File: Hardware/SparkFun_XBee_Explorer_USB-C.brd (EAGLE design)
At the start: 35.6 x 59.7 mm, 106 parts, among them J3 USB Female Type C Connector, J4 QWIIC_RIGHT_ANGLE, U2 AP63203, U5 ESD Diode, U7 FT231XS

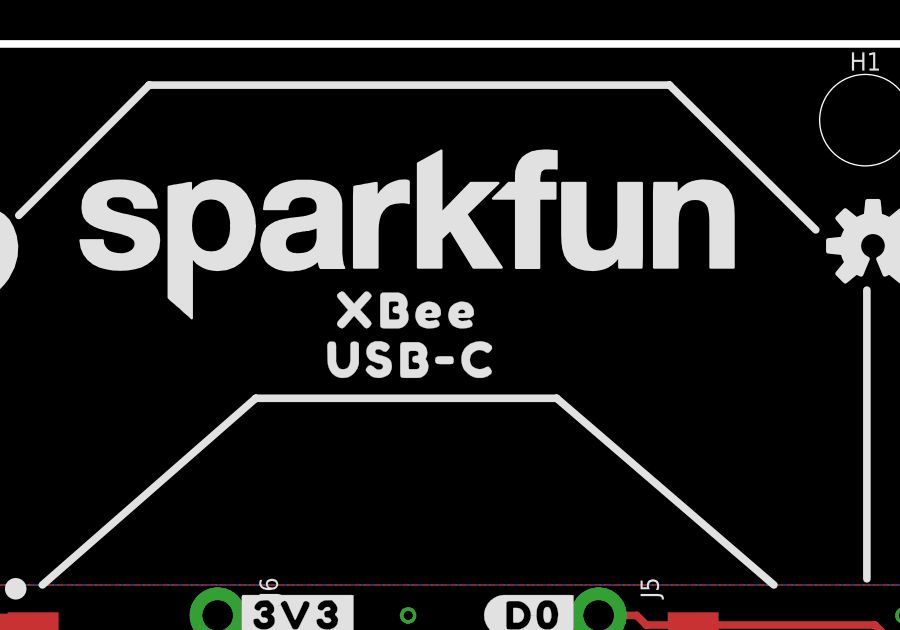
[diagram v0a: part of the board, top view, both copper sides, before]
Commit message: Adds "Explorer" to silk
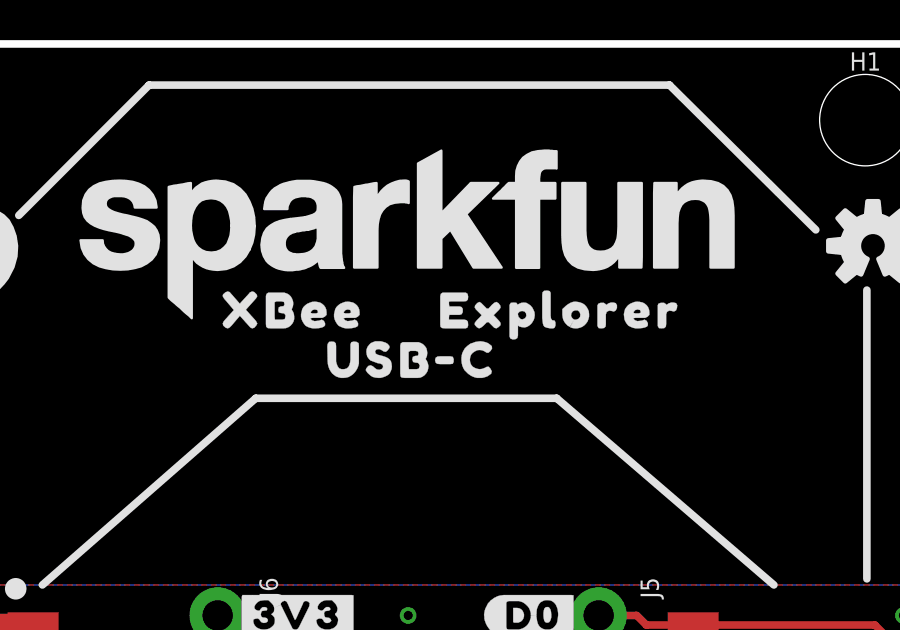
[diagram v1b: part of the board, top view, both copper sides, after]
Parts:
- added U$31, U$32: (no value), top:EXPLORER1344
- moved U$10 3.81 mm to (14.0, 50.8)
- moved U$23 3.81 mm to (21.6, 50.8)
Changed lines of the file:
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@@
 <layers>
 <layer number="1" name="Top" color="4" fill="1" visible="yes" active="yes"/>
-<layer number="2" name="Route2" color="23" fill="1" visible="yes" active="yes"/>
-<layer number="15" name="Route15" color="39" fill="1" visible="yes" active="yes"/>
+<layer number="2" name="Route2" color="23" fill="1" visible="no" active="yes"/>
+<layer number="15" name="Route15" color="39" fill="1" visible="no" active="yes"/>
 <layer number="16" name="Bottom" color="3" fill="1" visible="yes" active="yes"/>
 <layer number="17" name="Pads" color="26" fill="1" visible="yes" active="yes"/>
@@
 <element name="U$3" library="topmirror" package="#GND#0" value="" x="8.763" y="17.78" smashed="yes"/>
 <element name="LOGO1" library="SparkFun-Aesthetics" package="SFE_LOGO_NAME_.2" value="SFE_LOGO_NAME.2_INCH" x="17.78" y="53.34" smashed="yes"/>
-<element name="U$10" library="top" package="XBEE340" value="" x="17.78" y="50.8" smashed="yes"/>
-<element name="U$23" library="top" package="XBEE340" value="" x="17.78" y="50.8" smashed="yes" rot="MR0"/>
+<element name="U$10" library="top" package="XBEE340" value="" x="13.97" y="50.8" smashed="yes"/>
+<element name="U$23" library="top" package="XBEE340" value="" x="21.59" y="50.8" smashed="yes" rot="MR0"/>
 <element name="U$29" library="top" package="ASC32" value="" x="21.209" y="2.413" smashed="yes" rot="R90"/>
 <element name="U$1" library="top" package="RSSI31" value="" x="16.129" y="2.413" smashed="yes" rot="R90"/>
@@
 <element name="LOGO4" library="SparkFun-Aesthetics" package="ORDERING_INSTRUCTIONS" value="SPECIAL_INSTRUCTIONS-ORDERING" x="44.45" y="59.69" smashed="yes"/>
 <element name="U$11" library="topmirror" package="#D1#AD1#SCL#8" value="" x="29.718" y="38.1" smashed="yes" rot="MR0"/>
+<element name="U$31" library="top" package="EXPLORER1344" value="" x="22.86" y="50.8" smashed="yes"/>
+<element name="U$32" library="top" package="EXPLORER1344" value="" x="12.7" y="50.8" smashed="yes" rot="MR0"/>
 </elements>
 <signals>

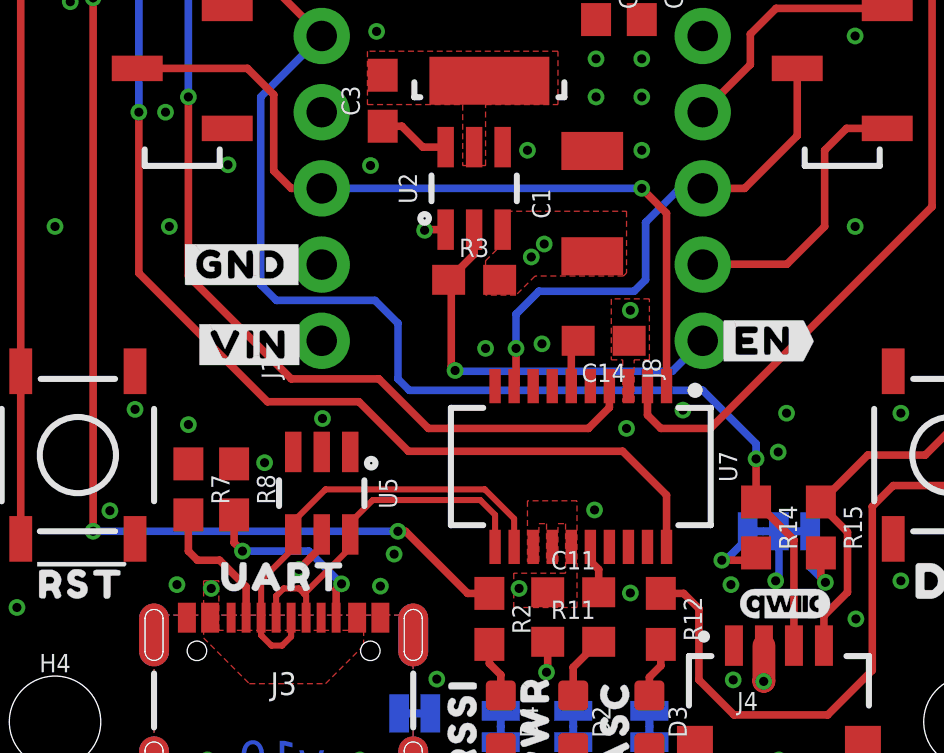
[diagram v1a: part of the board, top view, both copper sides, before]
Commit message: Adds 4.7uF decoupling cap to FTDI
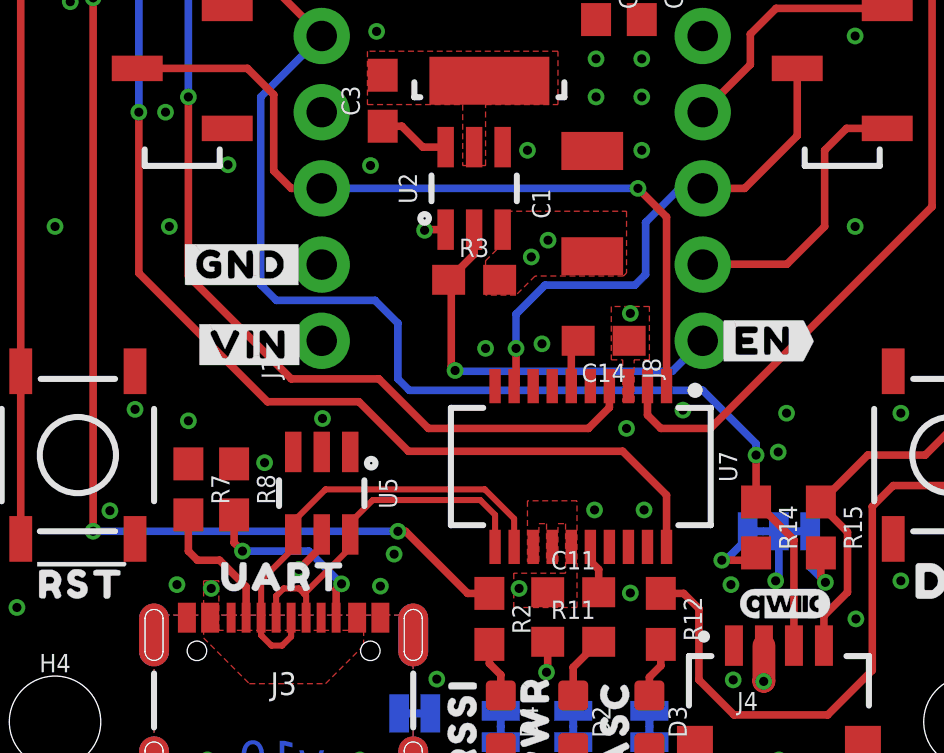
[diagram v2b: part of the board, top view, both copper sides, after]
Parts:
- moved FRAME1 10.2 mm to (-10.2, -26.7)
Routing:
- net GND: vias 74 -> 75
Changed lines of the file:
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@@
 <setting verticaltext="up"/>
 </settings>
-<grid distance="0.05" unitdist="inch" unit="inch" style="dots" multiple="1" display="yes" altdistance="0.005" altunitdist="inch" altunit="inch"/>
+<grid distance="0.05" unitdist="inch" unit="inch" style="dots" multiple="1" display="yes" altdistance="0.001" altunitdist="inch" altunit="inch"/>
 <layers>
 <layer number="1" name="Top" color="4" fill="1" visible="yes" active="yes"/>
-<layer number="2" name="Route2" color="23" fill="1" visible="no" active="yes"/>
-<layer number="15" name="Route15" color="39" fill="1" visible="no" active="yes"/>
+<layer number="2" name="Route2" color="23" fill="1" visible="yes" active="yes"/>
+<layer number="15" name="Route15" color="39" fill="1" visible="yes" active="yes"/>
 <layer number="16" name="Bottom" color="3" fill="1" visible="yes" active="yes"/>
 <layer number="17" name="Pads" color="26" fill="1" visible="yes" active="yes"/>
@@
 <layer number="45" name="Holes" color="7" fill="1" visible="yes" active="yes"/>
 <layer number="46" name="Milling" color="3" fill="1" visible="no" active="yes"/>
-<layer number="47" name="Measures" color="7" fill="1" visible="no" active="yes"/>
+<layer number="47" name="Measures" color="7" fill="1" visible="yes" active="yes"/>
 <layer number="48" name="Document" color="7" fill="1" visible="no" active="yes"/>
 <layer number="49" name="Reference" color="13" fill="1" visible="yes" active="yes"/>
@@
 <wire x1="35.56" y1="0" x2="35.56" y2="59.69" width="0.254" layer="20"/>
 <wire x1="35.56" y1="59.69" x2="0" y2="59.69" width="0.254" layer="20"/>
-<text x="17.78" y="-36.83" size="1.778" layer="51" font="vector">Elias Santistevan</text>
+<text x="17.78" y="-26.67" size="1.778" layer="51" font="vector">Elias Santistevan</text>
 <text x="-19.05" y="-8.89" size="1.778" layer="47" font="vector" ratio="15">Units in Inches</text>
 <text x="11.557" y="0.635" size="1.27" layer="16" font="vector" ratio="15" rot="MR0">v10</text>
@@
 <text x="20.193" y="37.211" size="1.778" layer="15" font="vector" ratio="15">3</text>
 <text x="22.733" y="37.211" size="1.778" layer="16" font="vector" ratio="15" rot="SMR0">4</text>
+<dimension x1="0" y1="0" x2="26.67" y2="0" x3="13.335" y3="-15.24" textsize="1.778" textratio="15" layer="47" unit="inch"/>
+<dimension x1="32.385" y1="11.43" x2="35.56" y2="11.43" x3="33.9725" y3="-3.81" textsize="1.778" textratio="15" layer="47" unit="inch"/>
 </plain>
 <attributes>
@@
 <attribute name="VALUE" x="8.89" y="10.16" size="0.6096" layer="27" font="vector" ratio="20" rot="R270" align="bottom-center"/>
 </element>
-<element name="FRAME1" library="SparkFun-Aesthetics" package="CREATIVE_COMMONS" value="FRAME-LEDGER" x="-10.16" y="-36.83" smashed="yes">
-<attribute name="DESIGNER" value="" x="-10.16" y="-36.83" size="1.778" layer="27" display="off"/>
-<attribute name="REV" value="" x="-10.16" y="-36.83" size="1.778" layer="27" display="off"/>
+<element name="FRAME1" library="SparkFun-Aesthetics" package="CREATIVE_COMMONS" value="FRAME-LEDGER" x="-10.16" y="-26.67" smashed="yes">
+<attribute name="DESIGNER" value="" x="-10.16" y="-26.67" size="1.778" layer="27" display="off"/>
+<attribute name="REV" value="" x="-10.16" y="-26.67" size="1.778" layer="27" display="off"/>
 </element>
 <element name="U$4" library="topmirror" package="#SHLD#36" value="" x="11.049" y="2.794" smashed="yes" rot="MR0"/>
@@
 <wire x1="27.17" y1="8.605" x2="25.908" y2="9.867" width="0.254" layer="1"/>
 <wire x1="24.13" y1="13.589" x2="14.351" y2="13.589" width="0.254" layer="16"/>
-<wire x1="25.908" y1="9.867" x2="25.908" y2="11.303" width="0.254" layer="1"/>
-<via x="25.908" y="11.303" extent="1-16" drill="0.3048"/>
+<wire x1="25.908" y1="9.867" x2="25.908" y2="11.43" width="0.254" layer="1"/>
+<via x="25.908" y="11.43" extent="1-16" drill="0.3048"/>
 <wire x1="24.13" y1="13.589" x2="25.908" y2="11.811" width="0.254" layer="16"/>
-<wire x1="25.908" y1="11.811" x2="25.908" y2="11.303" width="0.254" layer="16"/>
+<wire x1="25.908" y1="11.811" x2="25.908" y2="11.43" width="0.254" layer="16"/>
 <wire x1="9.91950625" y1="16.5862" x2="9.398" y2="17.10770625" width="0.254" layer="16"/>
 <wire x1="9.398" y1="23.368" x2="11.43" y2="25.4" width="0.254" layer="16"/>
@@
 <via x="3.048" y="26.543" extent="1-16" drill="0.3048"/>
 <via x="11.4554" y="12.6492" extent="1-16" drill="0.3048"/>
-<via x="6.985" y="12.446" extent="1-16" drill="0.3048"/>
+<via x="6.985" y="12.573" extent="1-16" drill="0.3048"/>
 <via x="9.525" y="11.176" extent="1-16" drill="0.3048"/>
 <via x="17.78" y="40.64" extent="1-16" drill="0.3048"/>
@@
 <via x="6.604" y="7.112" extent="1-16" drill="0.3048"/>
 <via x="26.924" y="12.827" extent="1-16" drill="0.3048"/>
+<via x="22.1742" y="9.6012" extent="1-16" drill="0.3048"/>
 </signal>
 <signal name="3.3V">
@@
 <vertex x="21.844" y="14.605"/>
 <vertex x="22.352" y="14.605"/>
-<vertex x="22.352" y="16.637"/>
-<vertex x="21.082" y="16.637"/>
+<vertex x="22.352" y="16.383"/>
+<vertex x="21.082" y="16.383"/>
 <vertex x="21.082" y="14.605"/>
 <vertex x="21.463" y="14.605"/>
@@
 <wire x1="26.67" y1="7.3486" x2="26.5604" y2="7.239" width="0.254" layer="16"/>
 <via x="26.5604" y="7.239" extent="1-16" drill="0.3048"/>
-<via x="21.717" y="16.256" extent="1-16" drill="0.3048"/>
+<via x="21.717" y="16.1544" extent="1-16" drill="0.3048"/>
 <wire x1="26.17" y1="5.08" x2="26.17" y2="3.8942" width="0.762" layer="1"/>
 <wire x1="26.17" y1="3.8942" x2="26.162" y2="3.8862" width="0.762" layer="1"/>
@@
 <wire x1="3.81" y1="8.89" x2="3.81" y2="26.67" width="0.254" layer="1"/>
 <via x="3.81" y="26.67" extent="1-16" drill="0.3048"/>
-<wire x1="4.064" y1="27.178" x2="3.81" y2="26.924" width="0.254" layer="2"/>
-<wire x1="3.81" y1="26.67" x2="3.81" y2="26.924" width="0.254" layer="2"/>
+<wire x1="3.937" y1="27.178" x2="3.81" y2="27.051" width="0.254" layer="2"/>
+<wire x1="3.81" y1="26.67" x2="3.81" y2="27.051" width="0.254" layer="2"/>
 <wire x1="9.398" y1="27.94" x2="11.43" y2="27.94" width="0.254" layer="2"/>
-<wire x1="4.064" y1="27.178" x2="8.636" y2="27.178" width="0.254" layer="2"/>
+<wire x1="3.937" y1="27.178" x2="8.636" y2="27.178" width="0.254" layer="2"/>
 <wire x1="8.636" y1="27.178" x2="9.398" y2="27.94" width="0.254" layer="2"/>
 </signal>
@@
 <wire x1="9.8298" y1="23.4442" x2="8.954" y2="24.32" width="0.254" layer="1"/>
 <wire x1="8.954" y1="24.32" x2="5.28" y2="24.32" width="0.254" layer="1"/>
-<wire x1="22.9235" y1="13.7287" x2="22.9235" y2="19.4945" width="0.254" layer="1"/>
-<wire x1="22.9235" y1="19.4945" x2="22.098" y2="20.32" width="0.254" layer="1"/>
-<via x="22.098" y="20.32" extent="1-16" drill="0.3048"/>
-<wire x1="22.098" y1="20.32" x2="11.43" y2="20.32" width="0.254" layer="16"/>
+<wire x1="22.9235" y1="13.7287" x2="22.9235" y2="19.3675" width="0.254" layer="1"/>
+<wire x1="22.9235" y1="19.3675" x2="21.971" y2="20.32" width="0.254" layer="1"/>
+<via x="21.971" y="20.32" extent="1-16" drill="0.3048"/>
+<wire x1="21.971" y1="20.32" x2="11.43" y2="20.32" width="0.254" layer="16"/>
 </signal>
 <signal name="D4/SPI_PICO">
@@
 <wire x1="17.907" y1="14.986" x2="17.907" y2="13.7922" width="0.254" layer="1"/>
 <via x="17.907" y="14.986" extent="1-16" drill="0.3048"/>
-<wire x1="18.669" y1="16.891" x2="17.907" y2="16.129" width="0.254" layer="16"/>
+<wire x1="18.8722" y1="17.0942" x2="17.907" y2="16.129" width="0.254" layer="16"/>
 <wire x1="17.907" y1="14.986" x2="17.907" y2="16.129" width="0.254" layer="16"/>
-<wire x1="18.669" y1="16.891" x2="21.844" y2="16.891" width="0.254" layer="16"/>
-<wire x1="21.844" y1="16.891" x2="22.225" y2="17.272" width="0.254" layer="16"/>
+<wire x1="18.8722" y1="17.0942" x2="21.8694" y2="17.0942" width="0.254" layer="16"/>
+<wire x1="21.8694" y1="17.0942" x2="22.225" y2="17.4498" width="0.254" layer="16"/>
 <wire x1="23.36034375" y1="20.32" x2="24.13" y2="20.32" width="0.254" layer="16"/>
-<wire x1="22.225" y1="17.272" x2="22.225" y2="19.18465625" width="0.254" layer="16"/>
+<wire x1="22.225" y1="17.4498" x2="22.225" y2="19.18465625" width="0.254" layer="16"/>
 <wire x1="22.225" y1="19.18465625" x2="23.36034375" y2="20.32" width="0.254" layer="16"/>
 </signal>
@@
 <via x="7.747" y="6.985" extent="1-16" drill="0.3048"/>
 <via x="10.668" y="7.62" extent="1-16" drill="0.3048"/>
-<wire x1="11.049" y1="8.001" x2="10.668" y2="7.62" width="0.254" layer="1"/>
 <wire x1="10.668" y1="7.62" x2="7.747" y2="7.62" width="0.254" layer="15"/>
-<via x="18.8468" y="18.4658" extent="1-16" drill="0.3048"/>
-<wire x1="18.415" y1="18.034" x2="18.8468" y2="18.4658" width="0.762" layer="15"/>
+<via x="18.9738" y="18.5928" extent="1-16" drill="0.3048"/>
+<wire x1="18.415" y1="18.034" x2="18.9738" y2="18.5928" width="0.762" layer="15"/>
 <polygon width="0.127" layer="1" thermals="no">
 <vertex x="16.891" y="16.764"/>
@@
 </polygon>
 <wire x1="11.43" y1="8.7849" x2="11.43" y2="8.382" width="0.254" layer="1"/>
-<wire x1="11.43" y1="8.382" x2="11.049" y2="8.001" width="0.254" layer="1"/>
+<wire x1="11.43" y1="8.382" x2="10.668" y2="7.62" width="0.254" layer="1"/>
 </signal>
 </signals>

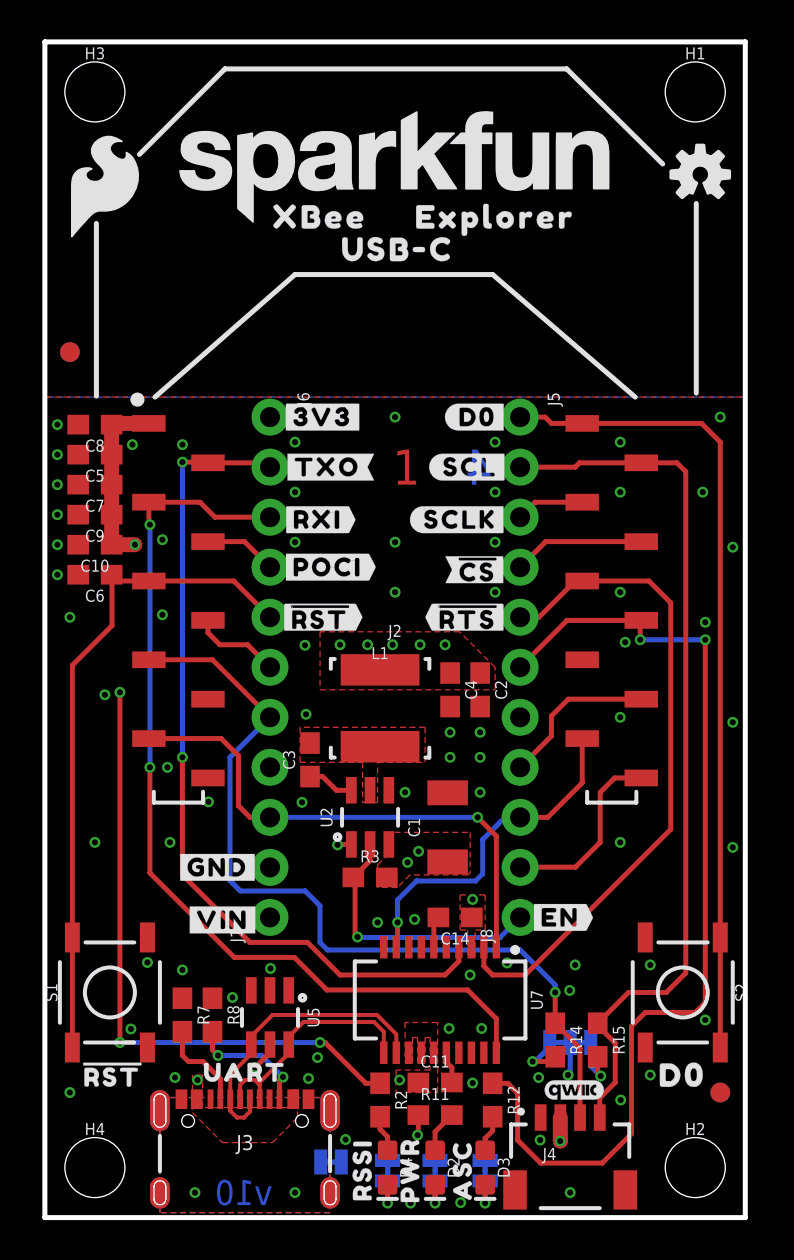
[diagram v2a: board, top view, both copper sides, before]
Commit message: Fixes anchors on some title labels in the schematic, adds more vias
* Increases the size of the Qwiic logo
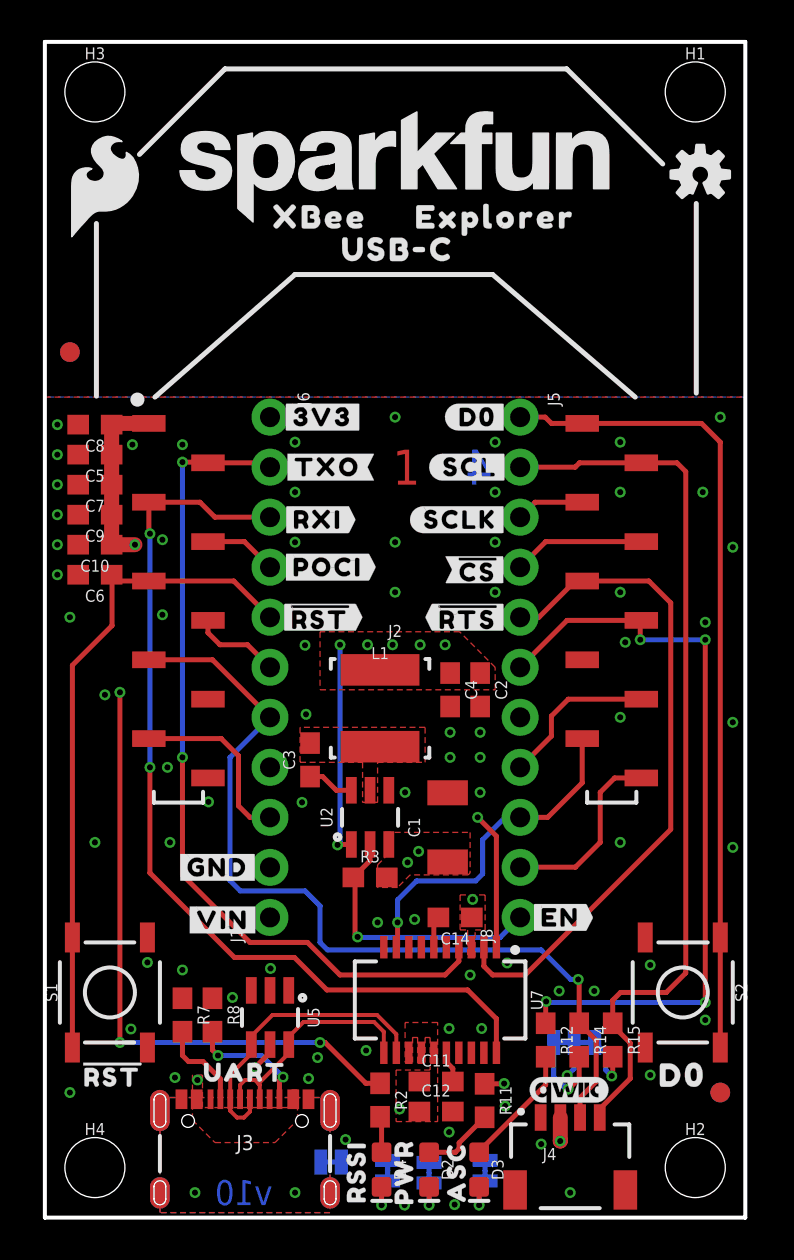
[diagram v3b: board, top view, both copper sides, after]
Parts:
- added C12: 4.7uF, SparkFun-Capacitors:0603
- LOGO3: value QWIIC_LOGO_3MM -> QWIIC_LOGO_4MM; device SparkFun-Aesthetics:QWIIC_3MM -> SparkFun-Aesthetics:QWIIC_4MM
- moved R12 4.07 mm to (25.4, 9.02)
- moved R11 2.62 mm to (22.3, 5.94), turned to 270 degrees
- moved R14 1.22 mm to (27.1, 9.02)
- moved R15 0.76 mm to (28.8, 9.02)
- moved U$1 0.32 mm to (15.8, 2.31)
- moved D2 0.32 mm to (19.5, 2.44)
- moved D3 0.32 mm to (22.0, 2.44)
- moved D4 0.32 mm to (17.1, 2.44)
- moved PLED 0.32 mm to (19.5, 2.28)
- moved U$2 0.32 mm to (18.2, 2.31)
- moved U$29 0.32 mm to (20.9, 2.31)
- moved LOGO3 0.25 mm to (26.6, 6.48)
- moved U$26 0.25 mm to (26.9, 10.5)
- moved I2C_PU 0.20 mm to (26.9, 8.89)
- moved C11 0.07 mm to (19.9, 6.91)
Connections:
- net 3.3V: now also C12.1
- net GND: now also C12.2
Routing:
- net D5/ASSOCIATE: track 50.3 -> 39.1 mm, vias 2 -> 4
- net N$12: track 1.86 -> 6.25 mm
- net N$11: track 2.64 -> 4.62 mm
- net N$7: track 2.14 -> 3.73 mm
- net D11/SDA: track 43.5 -> 45.1 mm
